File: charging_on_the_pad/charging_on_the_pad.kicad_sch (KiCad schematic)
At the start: 36 parts, among them J2 Conn_01x06, J3 Conn_01x05_Female, U1 PIC18F26K83, U2 MCP2562, Y1 12 MHz

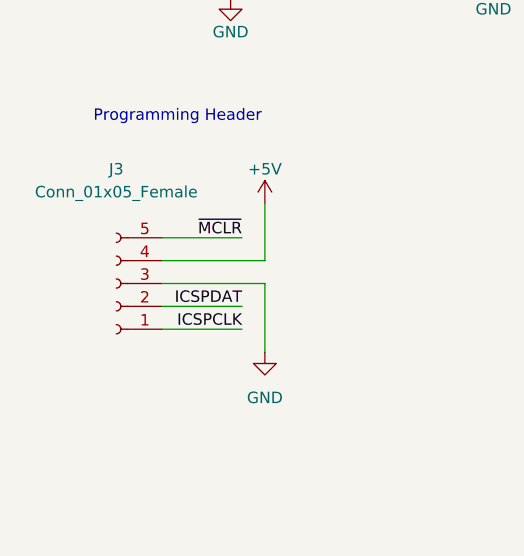
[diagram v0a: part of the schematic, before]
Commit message: add new buck and update schematic to match
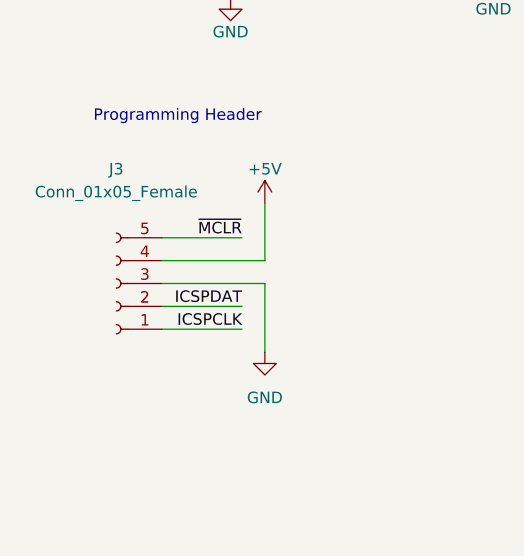
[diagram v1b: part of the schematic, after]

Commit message: added motor connectors and allocated pins
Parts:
- added J1: Conn_01x04_Socket, symbol Connector:Conn_01x04_Socket
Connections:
- net +13V: now also J1.4 (Pin_4)
- net GND: now also J1.1 (Pin_1)
- net MOTOR_INPUT: now reaches U1.21 (RB0)
- net MOTOR_INPUT: now also J1.3 (Pin_3)
- net MOTOR_OUTPUT: now reaches U1.22 (RB1)
- net MOTOR_OUTPUT: now also J1.2 (Pin_2)
- no-connect marks 8 -> 6
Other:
- note added: "2023/11/26"
- note added: "3"
- note added: "Motor Control"
- note removed: "2"
- note removed: "2023/04/05"
- moved on the sheet: H1, H2, H3, H4

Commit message: fuse to smd for real this time, netlabel connection points fixed, motor now connected to +BATT rather than +13V
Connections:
- net +13V: no longer J1.4 (Pin_4)
- net +BATT: now also J1.4 (Pin_4)
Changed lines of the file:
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@@
     (stroke (width 0) (type default))
   )
-  (wire (pts (xy 161.29 68.58) (xy 176.53 68.58))
+  (wire (pts (xy 161.29 68.58) (xy 177.8 68.58))
     (stroke (width 0) (type default))
   )
@@
     (stroke (width 0) (type default))
   )
-  (wire (pts (xy 161.29 71.12) (xy 176.53 71.12))
+  (wire (pts (xy 161.29 71.12) (xy 177.8 71.12))
     (stroke (width 0) (type default))
   )
@@
     (effects (font (size 1.27 1.27)) (justify right bottom))
   )
+  (label "MOTOR_INPUT" (at 104.14 180.34 180) (fields_autoplaced)
+    (effects (font (size 1.27 1.27)) (justify right bottom))
+  )
+  (label "MOTOR_OUTPUT" (at 104.14 182.88 180) (fields_autoplaced)
+    (effects (font (size 1.27 1.27)) (justify right bottom))
+  )
   (label "ICSPCLK" (at 171.45 55.88 180) (fields_autoplaced)
     (effects (font (size 1.27 1.27)) (justify right bottom))
@@
     (effects (font (size 1.27 1.27)) (justify left bottom))
   )
+  (label "MOTOR_INPUT" (at 177.8 71.12 180) (fields_autoplaced)
+    (effects (font (size 1.27 1.27)) (justify right bottom))
+  )
   (label "BATT_VSENSE" (at 111.76 78.74 0) (fields_autoplaced)
     (effects (font (size 1.27 1.27)) (justify left bottom))
@@
     (effects (font (size 1.27 1.27)) (justify left bottom))
   )
-  (label "MOTOR_OUTPUT" (at 161.29 68.58 0) (fields_autoplaced)
-    (effects (font (size 1.27 1.27)) (justify left bottom))
-  )
-  (label "MOTOR_INPUT" (at 161.29 71.12 0) (fields_autoplaced)
-    (effects (font (size 1.27 1.27)) (justify left bottom))
+  (label "MOTOR_OUTPUT" (at 177.8 68.58 180) (fields_autoplaced)
+    (effects (font (size 1.27 1.27)) (justify right bottom))
   )
   (label "CAN_TX" (at 205.74 138.43 0) (fields_autoplaced)
@@
     (effects (font (size 1.27 1.27)) (justify left bottom))
   )
-  (label "MOTOR_OUTPUT" (at 88.9 182.88 0) (fields_autoplaced)
-    (effects (font (size 1.27 1.27)) (justify left bottom))
-  )
   (label "OSC1" (at 109.22 115.57 0) (fields_autoplaced)
     (effects (font (size 1.27 1.27)) (justify left bottom))
@@
   )
   (label "CAN_TX" (at 111.76 73.66 0) (fields_autoplaced)
-    (effects (font (size 1.27 1.27)) (justify left bottom))
-  )
-  (label "MOTOR_INPUT" (at 88.9 180.34 0) (fields_autoplaced)
     (effects (font (size 1.27 1.27)) (justify left bottom))
   )
@@
     )
   )
+  (symbol (lib_id "power:+BATT") (at 118.11 172.72 0) (mirror y) (unit 1)
+    (in_bom yes) (on_board yes) (dnp no)
+    (property "Reference" "#PWR021" (at 118.11 176.53 0)
+      (effects (font (size 1.27 1.27)) hide)
+    )
+    (property "Value" "+BATT" (at 118.11 167.64 0)
+      (effects (font (size 1.27 1.27)))
+    )
+    (property "Footprint" "" (at 118.11 172.72 0)
+      (effects (font (size 1.27 1.27)) hide)
+    )
+    (property "Datasheet" "" (at 118.11 172.72 0)
+      (effects (font (size 1.27 1.27)) hide)
+    )
+    (pin "1")
+    (instances
+      (project "charging_on_the_pad"
+        (path "/9538e4ed-27e6-4c37-b989-9859dc0d49e8"
+          (reference "#PWR021") (unit 1)
+        )
+      )
+    )
+  )
   (symbol (lib_id "Device:C") (at 81.28 128.27 270) (mirror x) (unit 1)
     (in_bom yes) (on_board yes) (dnp no) (fields_autoplaced)
@@
     )
   )
-  (symbol (lib_name "+13V_1") (lib_id "charging_on_the_pad:+13V") (at 118.11 172.72 0) (mirror y) (unit 1)
-    (in_bom no) (on_board no) (dnp no)
-    (property "Reference" "#U01" (at 110.49 170.18 0)
-      (effects (font (size 1.27 1.27)) hide)
-    )
-    (property "Value" "+13V" (at 121.285 167.64 0)
-      (effects (font (size 1.27 1.27)) (justify left))
-    )
-    (property "Footprint" "" (at 118.11 170.18 0)
-      (effects (font (size 1.27 1.27)) hide)
-    )
-    (property "Datasheet" "" (at 118.11 170.18 0)
-      (effects (font (size 1.27 1.27)) hide)
-    )
-    (pin "1")
-    (instances
-      (project "charging_on_the_pad"
-        (path "/9538e4ed-27e6-4c37-b989-9859dc0d49e8"
-          (reference "#U01") (unit 1)
-        )
-      )
-    )
-  )
   (symbol (lib_id "power:+BATT") (at 52.07 69.85 0) (mirror y) (unit 1)
-    (in_bom yes) (on_board yes) (dnp no) (fields_autoplaced)
+    (in_bom yes) (on_board yes) (dnp no)
     (property "Reference" "#PWR0110" (at 52.07 73.66 0)
       (effects (font (size 1.27 1.27)) hide)

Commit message: removed all CAN/VSENSE testpoints
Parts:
- removed TP1, TP2, TP3, TP4: TestPoint, TestPoint:TestPoint_Pad_D1.0mm, symbol Connector:TestPoint
- removed TP5, TP6: TestPoint, TestPoint:TestPoint_Pad_D2.0mm, symbol Connector:TestPoint
- renumbered TP7 to TP1, TP8 to TP2, TP9 to TP3, TP10 to TP4, TP11 to TP5, TP12 to TP6
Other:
- moved on the sheet: TP1, TP2, TP3, TP4, TP6

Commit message: fixed ICHG_EN, FET between +BATT and MOTOR_V, Resistor Divider on 13V buck
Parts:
- added Q7: BSS138, Package_TO_SOT_SMD:SOT-23_Handsoldering, symbol Transistor_FET:BSS138
- added R31: 10k, Resistor_SMD:R_0805_2012Metric_Pad1.20x1.40mm_HandSolder, symbol Device:R_US
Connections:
- net +BATT: now also Q7.3 (D); no longer J1.4 (Pin_4)
- net GND: now also R31.2
- net MOTOR_INPUT: now also Q7.1 (G), R31.1
- new net MOTOR_V: J1.4 (Pin_4), Q7.2 (S)
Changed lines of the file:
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@@
   (junction (at 52.07 78.74) (diameter 0) (color 0 0 0 0)
+  )
+  (junction (at 127 180.34) (diameter 0) (color 0 0 0 0)
   )
   (junction (at 177.8 125.73) (diameter 0) (color 0 0 0 0)
@@
     (stroke (width 0) (type default))
   )
+  (wire (pts (xy 88.9 177.8) (xy 119.38 177.8))
+    (stroke (width 0) (type default))
+  )
   (wire (pts (xy 124.46 55.88) (xy 102.87 55.88))
     (stroke (width 0) (type default))
@@
     (stroke (width 0) (type default))
   )
+  (wire (pts (xy 127 189.23) (xy 127 190.5))
+    (stroke (width 0) (type default))
+  )
   (wire (pts (xy 74.93 128.27) (xy 74.93 130.81))
     (stroke (width 0) (type default))
   )
-  (wire (pts (xy 118.11 172.72) (xy 118.11 177.8))
-    (stroke (width 0) (type default))
-  )
-  (wire (pts (xy 88.9 185.42) (xy 97.79 185.42))
+  (wire (pts (xy 88.9 185.42) (xy 104.14 185.42))
     (stroke (width 0) (type default))
   )
@@
     (stroke (width 0) (type default))
   )
-  (wire (pts (xy 88.9 180.34) (xy 104.14 180.34))
-    (stroke (width 0) (type default))
-  )
   (wire (pts (xy 142.24 123.19) (xy 149.86 123.19))
     (stroke (width 0) (type default))
@@
     (stroke (width 0) (type default))
   )
-  (wire (pts (xy 97.79 185.42) (xy 97.79 190.5))
+  (wire (pts (xy 104.14 185.42) (xy 104.14 190.5))
     (stroke (width 0) (type default))
   )
@@
     (stroke (width 0) (type default))
   )
+  (wire (pts (xy 88.9 180.34) (xy 127 180.34))
+    (stroke (width 0) (type default))
+  )
   (wire (pts (xy 40.64 128.27) (xy 35.56 128.27))
     (stroke (width 0) (type default))
   )
+  (wire (pts (xy 127 180.34) (xy 127 181.61))
+    (stroke (width 0) (type default))
+  )
   (wire (pts (xy 39.37 82.55) (xy 39.37 81.28))
     (stroke (width 0) (type default))
@@
     (stroke (width 0) (type default))
   )
-  (wire (pts (xy 88.9 177.8) (xy 118.11 177.8))
-    (stroke (width 0) (type default))
-  )
   (wire (pts (xy 99.06 54.61) (xy 99.06 58.42))
     (stroke (width 0) (type default))
   )
+  (wire (pts (xy 127 180.34) (xy 143.51 180.34))
+    (stroke (width 0) (type default))
+  )
   (wire (pts (xy 35.56 133.35) (xy 52.07 133.35))
     (stroke (width 0) (type default))
@@
   )
   (wire (pts (xy 44.45 123.19) (xy 44.45 115.57))
+    (stroke (width 0) (type default))
+  )
+  (wire (pts (xy 127 180.34) (xy 127 172.72))
     (stroke (width 0) (type default))
   )
@@
     (effects (font (size 1.27 1.27)) (justify right bottom))
   )
+  (label "GROUND" (at 104.14 185.42 180) (fields_autoplaced)
+    (effects (font (size 1.27 1.27)) (justify right bottom))
+  )
   (label "CANH" (at 40.64 128.27 180) (fields_autoplaced)
     (effects (font (size 1.27 1.27)) (justify right bottom))
   )
-  (label "MOTOR_INPUT" (at 104.14 180.34 180) (fields_autoplaced)
-    (effects (font (size 1.27 1.27)) (justify right bottom))
-  )
   (label "MOTOR_OUTPUT" (at 104.14 182.88 180) (fields_autoplaced)
     (effects (font (size 1.27 1.27)) (justify right bottom))
@@
     (effects (font (size 1.27 1.27)) (justify left bottom))
   )
+  (label "MOTOR_INPUT" (at 143.51 180.34 180) (fields_autoplaced)
+    (effects (font (size 1.27 1.27)) (justify right bottom))
+  )
   (label "CURR_13V" (at 214.63 134.62 0) (fields_autoplaced)
-    (effects (font (size 1.27 1.27)) (justify left bottom))
-  )
-  (label "POWER" (at 88.9 177.8 0) (fields_autoplaced)
     (effects (font (size 1.27 1.27)) (justify left bottom))
   )
@@
     (effects (font (size 1.27 1.27)) (justify right bottom))
   )
+  (label "MOTOR_V" (at 104.14 177.8 180) (fields_autoplaced)
+    (effects (font (size 1.27 1.27)) (justify right bottom))
+  )
   (label "ICSPDAT" (at 171.45 53.34 180) (fields_autoplaced)
     (effects (font (size 1.27 1.27)) (justify right bottom))
@@
     (effects (font (size 1.27 1.27)) (justify right bottom))
   )
-  (label "GROUND" (at 88.9 185.42 0) (fields_autoplaced)
-    (effects (font (size 1.27 1.27)) (justify left bottom))
-  )
   (label "ICSPDAT" (at 46.99 168.91 180) (fields_autoplaced)
     (effects (font (size 1.27 1.27)) (justify right bottom))
@@
     )
   )
-  (symbol (lib_id "power:GND") (at 97.79 190.5 0) (unit 1)
-    (in_bom yes) (on_board yes) (dnp no) (fields_autoplaced)
-    (property "Reference" "#PWR08" (at 97.79 196.85 0)
-      (effects (font (size 1.27 1.27)) hide)
-    )
-    (property "Value" "GND" (at 97.79 195.58 0)
-      (effects (font (size 1.27 1.27)))
-    )
-    (property "Footprint" "" (at 97.79 190.5 0)
-      (effects (font (size 1.27 1.27)) hide)
-    )
-    (property "Datasheet" "" (at 97.79 190.5 0)
+  (symbol (lib_id "power:GND") (at 104.14 190.5 0) (unit 1)
+    (in_bom yes) (on_board yes) (dnp no) (fields_autoplaced)
+    (property "Reference" "#PWR08" (at 104.14 196.85 0)
+      (effects (font (size 1.27 1.27)) hide)
+    )
+    (property "Value" "GND" (at 104.14 195.58 0)
+      (effects (font (size 1.27 1.27)))
+    )
+    (property "Footprint" "" (at 104.14 190.5 0)
+      (effects (font (size 1.27 1.27)) hide)
+    )
+    (property "Datasheet" "" (at 104.14 190.5 0)
       (effects (font (size 1.27 1.27)) hide)
     )
@@
         (path "/9538e4ed-27e6-4c37-b989-9859dc0d49e8"
           (reference "#PWR0117") (unit 1)
+        )
+      )
+    )
+  )
+  (symbol (lib_id "Transistor_FET:BSS138") (at 121.92 172.72 0) (mirror y) (unit 1)
+    (in_bom yes) (on_board yes) (dnp no)
+    (property "Reference" "Q7" (at 116.713 171.5516 0)
+      (effects (font (size 1.27 1.27)) (justify left))
+    )
+    (property "Value" "BSS138" (at 116.713 173.863 0)
+      (effects (font (size 1.27 1.27)) (justify left))
+    )
+    (property "Footprint" "Package_TO_SOT_SMD:SOT-23_Handsoldering" (at 116.84 174.625 0)
+      (effects (font (size 1.27 1.27) italic) (justify left) hide)
+    )
+    (property "Datasheet" "https://www.fairchildsemi.com/datasheets/BS/BSS138.pdf" (at 121.92 172.72 0)
+      (effects (font (size 1.27 1.27)) (justify left) hide)
+    )
+    (pin "3")
+    (pin "2")
+    (pin "1")
+    (instances
+      (project "charging_on_the_pad"
+        (path "/9538e4ed-27e6-4c37-b989-9859dc0d49e8"
+          (reference "Q7") (unit 1)
+        )
+      )
+      (project "remote_arming"
+        (path "/aad8b39b-7333-4e86-9fc9-e8cca3495ddc"
+          (reference "Q6") (unit 1)
         )
       )
@@
         (path "/9538e4ed-27e6-4c37-b989-9859dc0d49e8"
           (reference "#PWR0113") (unit 1)
+        )
+      )
+    )
+  )
+  (symbol (lib_id "power:+BATT") (at 119.38 167.64 0) (mirror y) (unit 1)
+    (in_bom yes) (on_board yes) (dnp no)
+    (property "Reference" "#PWR021" (at 119.38 171.45 0)
+      (effects (font (size 1.27 1.27)) hide)
+    )
+    (property "Value" "+BATT" (at 119.38 162.56 0)
+      (effects (font (size 1.27 1.27)))
+    )
+    (property "Footprint" "" (at 119.38 167.64 0)
+      (effects (font (size 1.27 1.27)) hide)
+    )
+    (property "Datasheet" "" (at 119.38 167.64 0)
+      (effects (font (size 1.27 1.27)) hide)
+    )
+    (pin "1")
+    (instances
+      (project "charging_on_the_pad"
+        (path "/9538e4ed-27e6-4c37-b989-9859dc0d49e8"
+          (reference "#PWR021") (unit 1)
         )
       )
@@
         (path "/9538e4ed-27e6-4c37-b989-9859dc0d49e8"
           (reference "#PWR0116") (unit 1)
+        )
+      )
+    )
+  )
+  (symbol (lib_id "Device:R_US") (at 127 185.42 0) (unit 1)
+    (in_bom yes) (on_board yes) (dnp no) (fields_autoplaced)
+    (property "Reference" "R31" (at 129.54 184.1499 0)
+      (effects (font (size 1.27 1.27)) (justify left))
+    )
+    (property "Value" "10k" (at 129.54 186.6899 0)
+      (effects (font (size 1.27 1.27)) (justify left))
+    )
+    (property "Footprint" "Resistor_SMD:R_0805_2012Metric_Pad1.20x1.40mm_HandSolder" (at 128.016 185.674 90)
+      (effects (font (size 1.27 1.27)) hide)
+    )
+    (property "Datasheet" "~" (at 127 185.42 0)
+      (effects (font (size 1.27 1.27)) hide)
+    )
+    (pin "1")
+    (pin "2")
+    (instances
+      (project "charging_on_the_pad"
+        (path "/9538e4ed-27e6-4c37-b989-9859dc0d49e8"
+          (reference "R31") (unit 1)
         )
       )
@@
     )
   )
-  (symbol (lib_id "power:+BATT") (at 118.11 172.72 0) (mirror y) (unit 1)
-    (in_bom yes) (on_board yes) (dnp no)
-    (property "Reference" "#PWR021" (at 118.11 176.53 0)
-      (effects (font (size 1.27 1.27)) hide)
-    )
-    (property "Value" "+BATT" (at 118.11 167.64 0)
-      (effects (font (size 1.27 1.27)))
-    )
-    (property "Footprint" "" (at 118.11 172.72 0)
-      (effects (font (size 1.27 1.27)) hide)
-    )
-    (property "Datasheet" "" (at 118.11 172.72 0)
-      (effects (font (size 1.27 1.27)) hide)
-    )
-    (pin "1")
-    (instances
-      (project "charging_on_the_pad"
-        (path "/9538e4ed-27e6-4c37-b989-9859dc0d49e8"
-          (reference "#PWR021") (unit 1)
-        )
-      )
-    )
-  )
   (symbol (lib_id "Device:C") (at 81.28 128.27 270) (mirror x) (unit 1)
     (in_bom yes) (on_board yes) (dnp no) (fields_autoplaced)
@@
         )
       )
+    )
+  )
+  (symbol (lib_id "power:GND") (at 127 190.5 0) (unit 1)
+    (in_bom yes) (on_board yes) (dnp no) (fields_autoplaced)
+    (property "Reference" "#PWR022" (at 127 196.85 0)
+      (effects (font (size 1.27 1.27)) hide)
+    )
+    (property "Value" "GND" (at 127 195.58 0)
+      (effects (font (size 1.27 1.27)))
+    )
+    (property "Footprint" "" (at 127 190.5 0)
+      (effects (font (size 1.27 1.27)) hide)
+    )
+    (property "Datasheet" "" (at 127 190.5 0)
+      (effects (font (size 1.27 1.27)) hide)
+    )
+    (pin "1")
+    (instances
+      (project "charging_on_the_pad"
+        (path "/9538e4ed-27e6-4c37-b989-9859dc0d49e8"
+          (reference "#PWR022") (unit 1)
+        )
+      )

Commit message: added more current sensing, fixed inductor
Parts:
- added C32: 0.1uF, Capacitor_SMD:C_0805_2012Metric_Pad1.18x1.45mm_HandSolder, symbol Device:C
- added C34: 1uF, Capacitor_SMD:C_0805_2012Metric_Pad1.18x1.45mm_HandSolder, symbol Device:C
- added R29, R30: 10R, Resistor_SMD:R_0805_2012Metric_Pad1.20x1.40mm_HandSolder, symbol Device:R_US
- added R37: 0.01R, Resistor_SMD:R_0805_2012Metric_Pad1.20x1.40mm_HandSolder, symbol Device:R_US
- added U8: INA180, Package_TO_SOT_SMD:SOT-23-5_HandSoldering, symbol canhw:INA180
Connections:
- net +5V: now also C32.1, U8.5 (VS)
- net GND: now also C32.2, U8.2 (GND)
- net MOTOR_INPUT: no longer J1.3 (Pin_3), Q7.1 (G), R31.1
- net MOTOR_V: now also R29.2, R37.2; no longer Q7.2 (S)
- net CURR_+BATT: now reaches U1.5 (RA3)
- new net: J1.3 (Pin_3), Q7.1 (G), R31.1
- new net: C34.1, R29.1, U8.4 (IN-)
- new net: C34.2, R30.2, U8.3 (IN+)
- new net CURR_MOTOR: U8.1 (VO)
- new net R_MOTOR_P: Q7.2 (S), R30.1, R37.1
- no-connect marks 6 -> 5
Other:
- sheet Power ports: added CURR_+BATT; removed none
- note added: "Motor Rail CSA (100V/V)"
- moved on the sheet: C1, C2, C4, H1, H2, H3, H4, J1, Q7, R31, TP1, TP2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

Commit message: added INA4180 chip and connections
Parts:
- removed C32: 0.1uF, Capacitor_SMD:C_0805_2012Metric_Pad1.18x1.45mm_HandSolder, symbol Device:C
- removed C34: 1uF, Capacitor_SMD:C_0805_2012Metric_Pad1.18x1.45mm_HandSolder, symbol Device:C
- removed R29, R30: 10R, Resistor_SMD:R_0805_2012Metric_Pad1.20x1.40mm_HandSolder, symbol Device:R_US
- removed U8: INA180, Package_TO_SOT_SMD:SOT-23-5_HandSoldering, symbol canhw:INA180
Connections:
- net CURR_MOTOR: now also U1.23 (RB2)
- no-connect marks 5 -> 4
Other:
- sheet Power ports: added CURR_MOTOR, R_MOTOR_N, R_MOTOR_P; removed none
- note removed: "Motor Rail CSA (100V/V)"

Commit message: fixed everything I believe?
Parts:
- added Q8: BSS138PW,115, Package_TO_SOT_SMD:SOT-23_Handsoldering, symbol Transistor_FET:BSS138
- added R27, R29: 10k, Resistor_SMD:R_0805_2012Metric_Pad1.20x1.40mm_HandSolder, symbol Device:R_US
- added R28: 120R, Resistor_SMD:R_0805_2012Metric_Pad1.20x1.40mm_HandSolder, symbol Device:R_US
- added R30: 1R, Resistor_SMD:R_0805_2012Metric_Pad1.20x1.40mm_HandSolder, symbol Device:R_US
- Q7: value BSS138 -> BSS138PW,115
- R31: value 10k -> 1R
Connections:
- net +BATT: now also R37.1, R29.1; no longer Q7.3 (D)
- net GND: now also Q8.2 (S), R27.2
- net MOTOR_INPUT: now also J1.3 (Pin_3)
- net MOTOR_OUTPUT: now also R30.1; no longer U1.22 (RB1)
- net MOTOR_V: now also Q7.2 (S); no longer R37.2
- net EN_MOTOR: now reaches U1.24 (RB3)
- net EN_MOTOR: now also R28.1
- removed net R_MOTOR_P: Q7.2 (S), R37.1
- new net: Q7.1 (G), Q8.3 (D), R29.2
- new net: Q8.1 (G), R27.1, R28.2
- new net MOTOR_OUT_CHIP: R30.2, R31.1, U1.22 (RB1)
- new net R_MOTOR_N: Q7.3 (D), R37.2
- no-connect marks 4 -> 3
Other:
- moved on the sheet: J1, Q7, R37
